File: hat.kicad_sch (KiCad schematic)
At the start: 6 parts, among them J1 GPIO, U1 CAT24C256

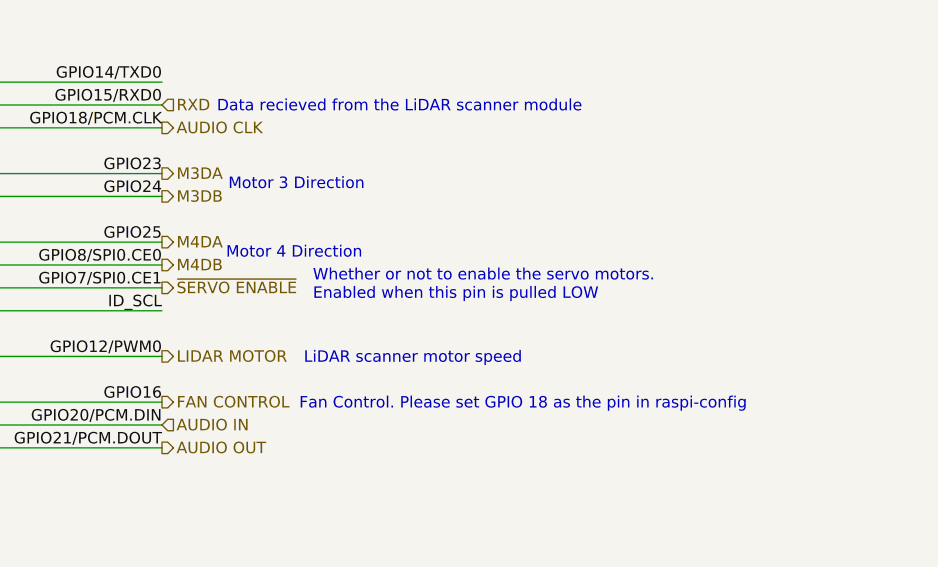
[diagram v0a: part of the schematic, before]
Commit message: feat: removed servo motors
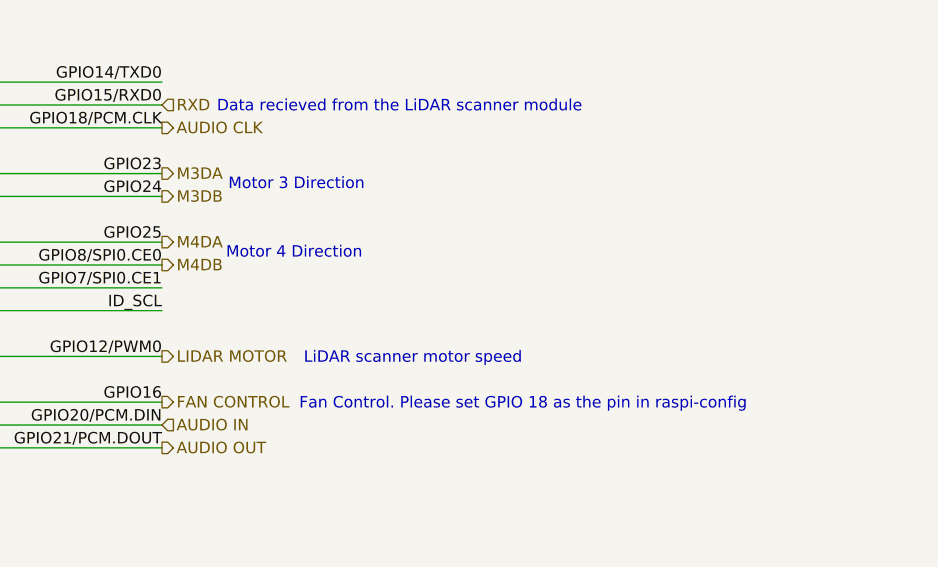
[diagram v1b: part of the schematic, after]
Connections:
- net ~{SERVO ENABLE} renamed GPIO7/SPI0.CE1
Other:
- note removed: "Whether or not to enable the servo motors. Enabled when this pin is pulled LOW"
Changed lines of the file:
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@@
-		)
-	)
-	(text "Whether or not to enable the servo motors.\nEnabled when this pin is pulled LOW"
-		(exclude_from_sim no)
-		(at 194.564 94.996 0)
-		(effects
-			(font
-				(size 1.27 1.27)
-			)
-			(justify left)
 		)
 	)
@@
 		)
 	)
-	(hierarchical_label "~{SERVO ENABLE}"
-		(shape output)
-		(at 177.8 95.25 0)
-		(effects
-			(font
-				(size 1.27 1.27)
-			)
-			(justify left)
-		)
-	)

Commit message: feat: wired up audio system
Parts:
- J1: Part# (none) -> C18078157
- JP1: now left out of the parts list
- R1, R2: Part# (none) -> C26042
- U1: footprint Package_SO:SOIC-8_3.9x4.9mm_P1.27mm -> Package_SO:SOP-8_3.76x4.96mm_P1.27mm; Part# (none) -> C36533643
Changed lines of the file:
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@@
+			)
+		)
+		(property "Part#" "C18078157"
+			(at 143.51 87.63 0)
+			(effects
+				(font
+					(size 1.27 1.27)
+				)
+				(hide yes)
 			)
 		)
@@
 			)
 		)
+		(property "Part#" ""
+			(at 67.31 179.07 0)
+			(effects
+				(font
+					(size 1.27 1.27)
+				)
+				(hide yes)
+			)
+		)
 		(pin "1"
 		)
@@
 			)
 		)
+		(property "Part#" "C26042"
+			(at 93.98 171.45 0)
+			(effects
+				(font
+					(size 1.27 1.27)
+				)
+				(hide yes)
+			)
+		)
 		(pin "1"
 		)
@@
 		(unit 1)
 		(exclude_from_sim no)
-		(in_bom yes)
+		(in_bom no)
 		(on_board yes)
 		(dnp no)
@@
 					(size 1.27 1.27)
 				)
+			)
+		)
+		(property "Part#" ""
+			(at 96.52 181.61 0)
+			(effects
+				(font
+					(size 1.27 1.27)
+				)
+				(hide yes)
 			)
 		)
@@
 			)
 		)
+		(property "Part#" "C26042"
+			(at 101.6 171.45 0)
+			(effects
+				(font
+					(size 1.27 1.27)
+				)
+				(hide yes)
+			)
+		)
 		(pin "1"
 		)
@@
 			)
 		)
-		(property "Footprint" "Package_SO:SOIC-8_3.9x4.9mm_P1.27mm"
+		(property "Footprint" "Package_SO:SOP-8_3.76x4.96mm_P1.27mm"
 			(at 81.28 179.07 0)
 			(effects
@@
 			)
 		)
+		(property "Part#" "C36533643"
+			(at 81.28 179.07 0)
+			(effects
+				(font
+					(size 1.27 1.27)
+				)
+				(hide yes)
+			)
+		)
